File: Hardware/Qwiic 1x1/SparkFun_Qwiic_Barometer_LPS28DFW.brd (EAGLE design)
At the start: 25.4 x 25.4 mm, 47 parts, among them J1 QWIIC_RIGHT_ANGLE, J2 QWIIC_RIGHT_ANGLE, U1 LPS28DFW

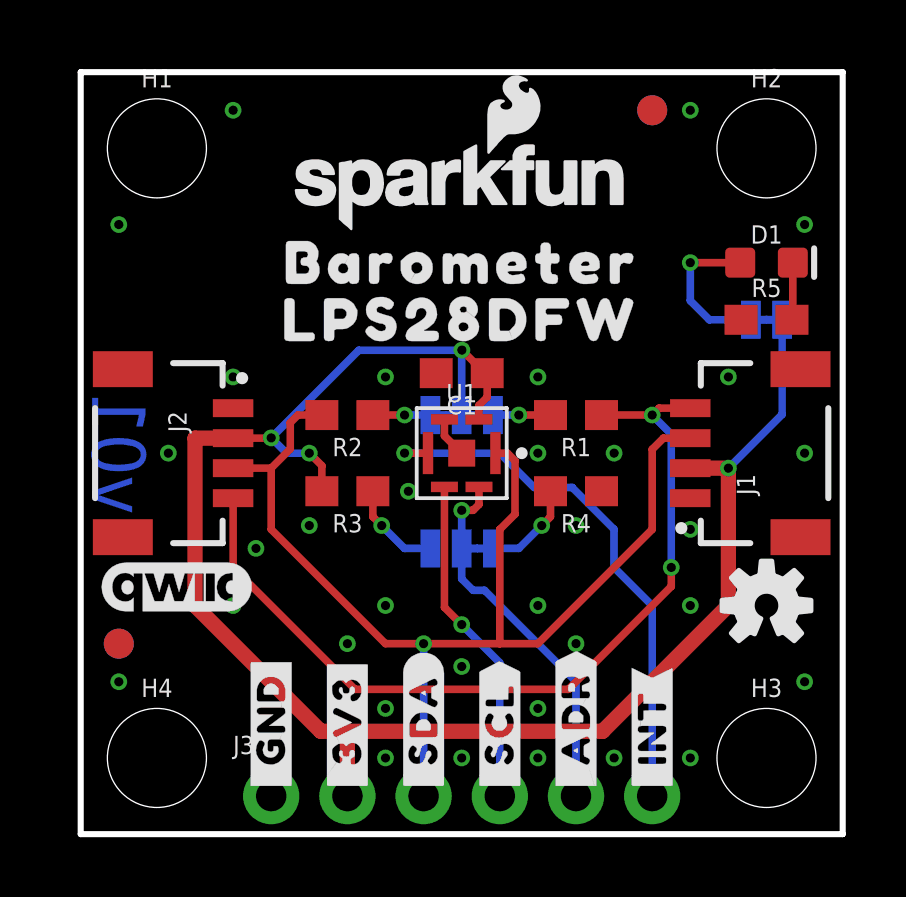
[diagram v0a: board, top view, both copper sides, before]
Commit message: Update 1x1 with mirrored LPS28DFW footprint
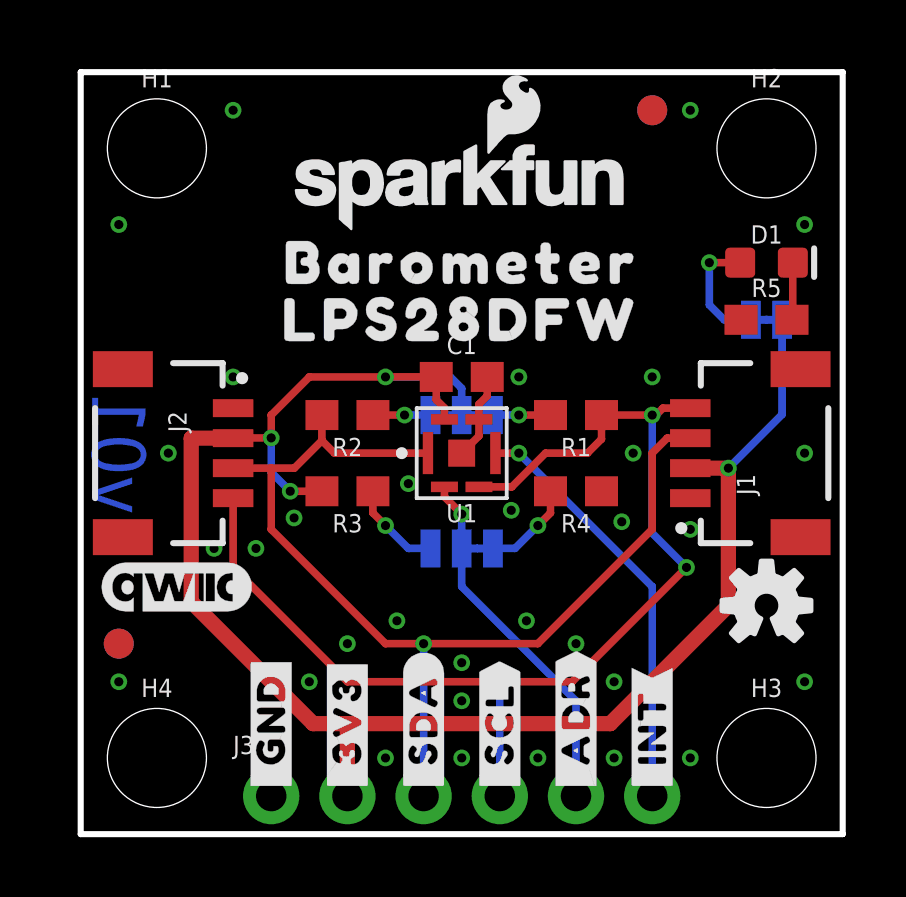
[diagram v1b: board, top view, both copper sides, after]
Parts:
- moved C1 0.13 mm to (12.7, 15.2), turned to 0 degrees
- turned U1 to 180 degrees
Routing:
- net INT: track 18.2 -> 14.1 mm
- net SDA: track 38.3 -> 34.9 mm
- net SCL: track 40.1 -> 38.5 mm, vias 4 -> 3
- net GND: track 1.36 -> 2.89 mm, vias 33 -> 32
- net N$4: track 5.22 -> 4.03 mm

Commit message: Design review updates
Add silk to PWR LED on 1x1
Tweak routing to use more T-junctions and route into side of pads rather than corners
Move via on I2C jumper silk of Micro
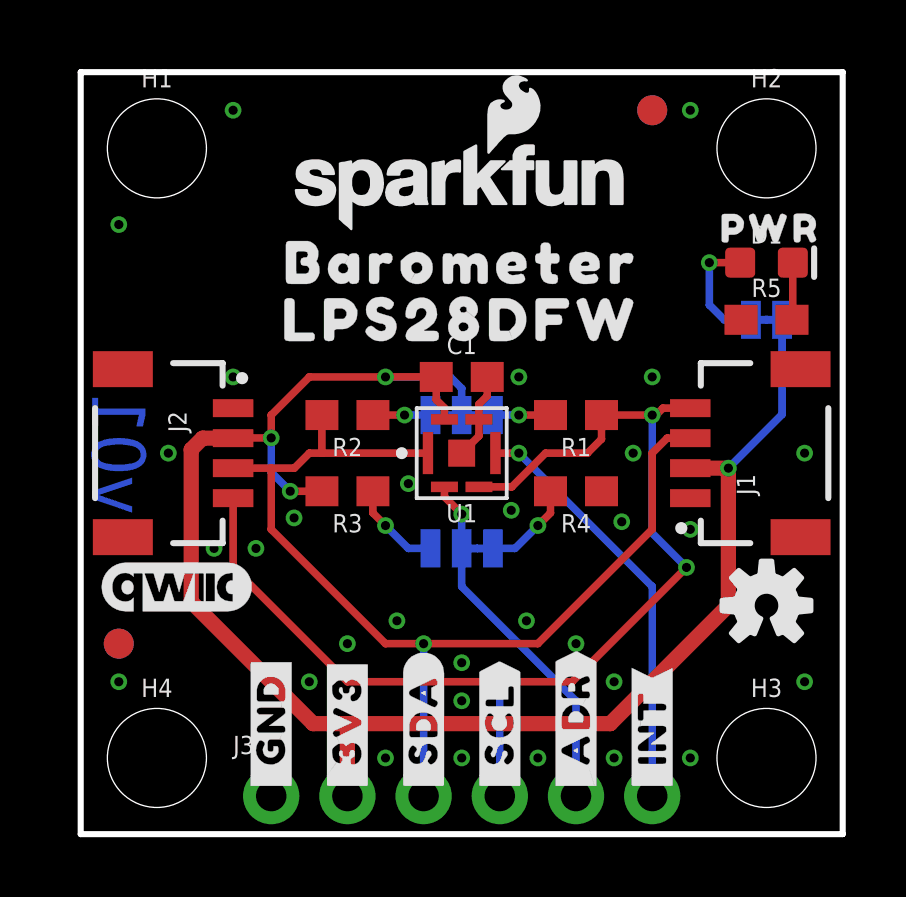
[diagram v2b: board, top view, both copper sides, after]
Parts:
- added U$18: (no value), output:PWR0
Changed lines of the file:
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@@
 <element name="U$22" library="output" package="#_ADR#0" value="" x="16.51" y="1.27" smashed="yes" rot="R90"/>
 <element name="U$23" library="output" package="#_ADR#0" value="" x="16.51" y="1.27" smashed="yes" rot="MR90"/>
+<element name="U$18" library="output" package="PWR0" value="" x="22.987" y="20.193" smashed="yes"/>
 </elements>
 <signals>
@@
 <contactref element="R3" pad="2"/>
 <contactref element="PWR" pad="2"/>
-<wire x1="5.08" y1="13.2" x2="3.683" y2="13.2" width="0.508" layer="1"/>
-<wire x1="3.683" y1="13.2" x2="3.683" y2="7.747" width="0.508" layer="1"/>
+<wire x1="5.08" y1="13.2" x2="4.064" y2="13.2" width="0.508" layer="1"/>
+<wire x1="4.064" y1="13.2" x2="3.683" y2="12.819" width="0.508" layer="1"/>
+<wire x1="3.683" y1="12.819" x2="3.683" y2="7.747" width="0.508" layer="1"/>
 <wire x1="3.683" y1="7.747" x2="7.747" y2="3.683" width="0.508" layer="1"/>
 <wire x1="17.653" y1="3.683" x2="21.59" y2="7.62" width="0.508" layer="1"/>
@@
 <wire x1="19.55" y1="13.2" x2="20.32" y2="13.2" width="0.254" layer="1"/>
 <wire x1="6.35" y1="12.2" x2="7.12" y2="12.2" width="0.254" layer="1"/>
-<wire x1="8.04" y1="13.12" x2="8.04" y2="13.97" width="0.254" layer="1"/>
-<wire x1="7.12" y1="12.2" x2="8.04" y2="13.12" width="0.254" layer="1"/>
-<wire x1="8.46" y1="12.7" x2="8.04" y2="13.12" width="0.254" layer="1"/>
-<wire x1="11.575" y1="12.7" x2="8.46" y2="12.7" width="0.254" layer="1"/>
+<wire x1="8.04" y1="13.97" x2="8.04" y2="12.7" width="0.254" layer="1"/>
+<wire x1="7.12" y1="12.2" x2="7.62" y2="12.7" width="0.254" layer="1"/>
+<wire x1="11.575" y1="12.7" x2="8.04" y2="12.7" width="0.254" layer="1"/>
+<wire x1="8.04" y1="12.7" x2="7.62" y2="12.7" width="0.254" layer="1"/>
 <wire x1="11.43" y1="1.27" x2="11.43" y2="6.35" width="0.254" layer="16"/>
 <via x="11.43" y="6.35" extent="1-16" drill="0.3048"/>
